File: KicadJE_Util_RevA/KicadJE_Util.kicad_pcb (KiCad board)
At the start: 2 copper layers, 268.5 x 128 mm, 225 parts, among them J101 Out1, J102 Out2, J103 In1.1, J104 In1.2, J105 In1.3, J106 SS_In2, J201 Out2.1, J202 Out2.2, J203 In2.1, J204 CV2.1, J205 In2.2, J206 CV2.2, J301 In3.1, J302 Out3.1, J303 Out3.2, P101 HEADER_2x5_Doepfer, P201 HEADER_2x5_Doepfer, P301 HEADER_2x5_Doepfer, U101 TL072, U102 TL072, U201 TL072, U202 TL072, U301 TL072, U302 TL072

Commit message: CV Module placed
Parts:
- added H201: ON, AJ:LED_Hole_3mm, F.Cu at (6.18, -1.42)
- added H202: MountingHole_Pad, AJ:MountingHole_Eurorack3, F.Cu at (-9.10, -1.15)
- added H203: MountingHole_Pad, AJ:MountingHole_Eurorack3, F.Cu at (1.95, -12.2)
- added H204: MountingHole_Pad, AJ:MountingHole_Eurorack3, F.Cu at (-1.10, -1.15)
- added H205: MountingHole_Pad, AJ:MountingHole_Eurorack3, F.Cu at (1.95, -7.20)
- added H302: MountingHole_Pad, AJ:MountingHole_Eurorack3, F.Cu at (24.9, -23.2)
- added H303: MountingHole_Pad, AJ:MountingHole_Eurorack3, F.Cu at (16.9, -18.2)
- added H304: MountingHole_Pad, AJ:MountingHole_Eurorack3, F.Cu at (24.9, -18.2)
- added H305: MountingHole_Pad, AJ:MountingHole_Eurorack3, F.Cu at (16.9, -23.2)
- added TP101: Tri, AJ:Jack_6m3, F.Cu at (70.4, -5.51)
- added TP104: In2, AJ:Jack_6m3, F.Cu at (59.3, -5.51)
- added TP106: SS, AJ:Jack_6m3, F.Cu at (48.3, -5.51)
- added TP108: OFF2, AJ:Pot_6m3_scale1, F.Cu at (50.8, -19.1)
- added TP109: Gain2, AJ:Pot_6m3_scale1, F.Cu at (82.9, -19.1)
- added TP110: Gain1, AJ:Pot_6m3_scale1, F.Cu at (66.8, -19.1)
- added TP201: Tri, AJ:Jack_6m3, F.Cu at (-7.57, -9.17)
- added TP202: SQ, AJ:Jack_6m3, F.Cu at (2.43, -20.2)
- added TP203: In1, AJ:Jack_6m3, F.Cu at (-18.6, -3.62)
- added TP204: In2, AJ:Jack_6m3, F.Cu at (-8.62, -20.2)
- added TP205: In3, AJ:Jack_6m3, F.Cu at (-29.7, -3.62)
- added TP206: SS, AJ:Jack_6m3, F.Cu at (-40.7, -3.62)
- added TP207: Glide1, AJ:Pot_6m3_scale1, F.Cu at (-22.2, -17.2)
- added TP208: Glide2, AJ:Pot_6m3_scale1, F.Cu at (-38.2, -17.2)
- J106: value SS_In2 -> In1.4
- TP107: value Gain -> OFF1
- moved R124 114.5 mm to (55.0, 82.0), turned to 90 degrees
- moved R123 105.8 mm to (75.5, 65.0)
- moved R126 102.0 mm to (55.0, 85.7), turned to 90 degrees
- moved R127 98.6 mm to (85.2, 85.7), turned to 90 degrees
- moved R112 98.2 mm to (64.5, 65.0), turned to 180 degrees
- moved C105 95.7 mm to (56.0, 95.2), turned to 90 degrees
- moved C103 94.5 mm to (76.0, 95.2), turned to 90 degrees
- moved R129 92.8 mm to (87.5, 96.3), turned to 270 degrees
- moved R131 92.1 mm to (87.5, 100.0), turned to 90 degrees
- moved R111 88.6 mm to (54.2, 104.0), turned to 90 degrees
- moved R128 85.9 mm to (67.5, 96.2), turned to 270 degrees
- moved R125 84.9 mm to (85.2, 82.0), turned to 90 degrees
- moved C106 84.0 mm to (84.0, 104.8), turned to 90 degrees
- moved R122 83.4 mm to (73.0, 104.0), turned to 90 degrees
- moved C104 81.1 mm to (64.2, 104.8), turned to 90 degrees
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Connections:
- RV101 pad 1: -12VA -> +12VA
- RV101 pad 3: +12VA -> -12VA
- RV103 pad 1: Net-(R127-Pad1) -> Inv2
- RV103 pad 3: Inv2 -> Net-(R127-Pad1)
- RV104 pad 1: -12VA -> +12VA
- RV104 pad 3: +12VA -> -12VA
- U101 pad 1: Out2 -> Net-(R128-Pad2)
- U101 pad 2: Net-(R117-Pad1) -> Inv1
- U101 pad 3: Net-(R122-Pad2) -> In1
- U102 pad 1: Net-(R128-Pad2) -> Net-(R129-Pad2)
- U102 pad 2: Inv1 -> Inv2
- U102 pad 3: In1 -> In2
- U102 pad 5: In2 -> Net-(R122-Pad2)
- U102 pad 6: Inv2 -> Net-(R117-Pad1)
- U102 pad 7: Net-(R129-Pad2) -> Out2
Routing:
- net +12VA: track 95.2 -> 76.5 mm
- net In3.1a: track 40.1 -> 25.1 mm, vias 2 -> 1
- net Out3.1: track 60.6 -> 47.5 mm
- net Net-(R316-Pad2): track 22.4 -> 10.1 mm
- net -12VA: track 80.6 -> 69.2 mm
- net Net-(R315-Pad2): track 5.28 -> 0.00 mm
- net In3.1: track 4.95 -> 0.00 mm
- net Net-(D304-Pad2): track 12.2 -> 8.72 mm
- net Net-(J303-PadT): track 10.7 -> 9.77 mm

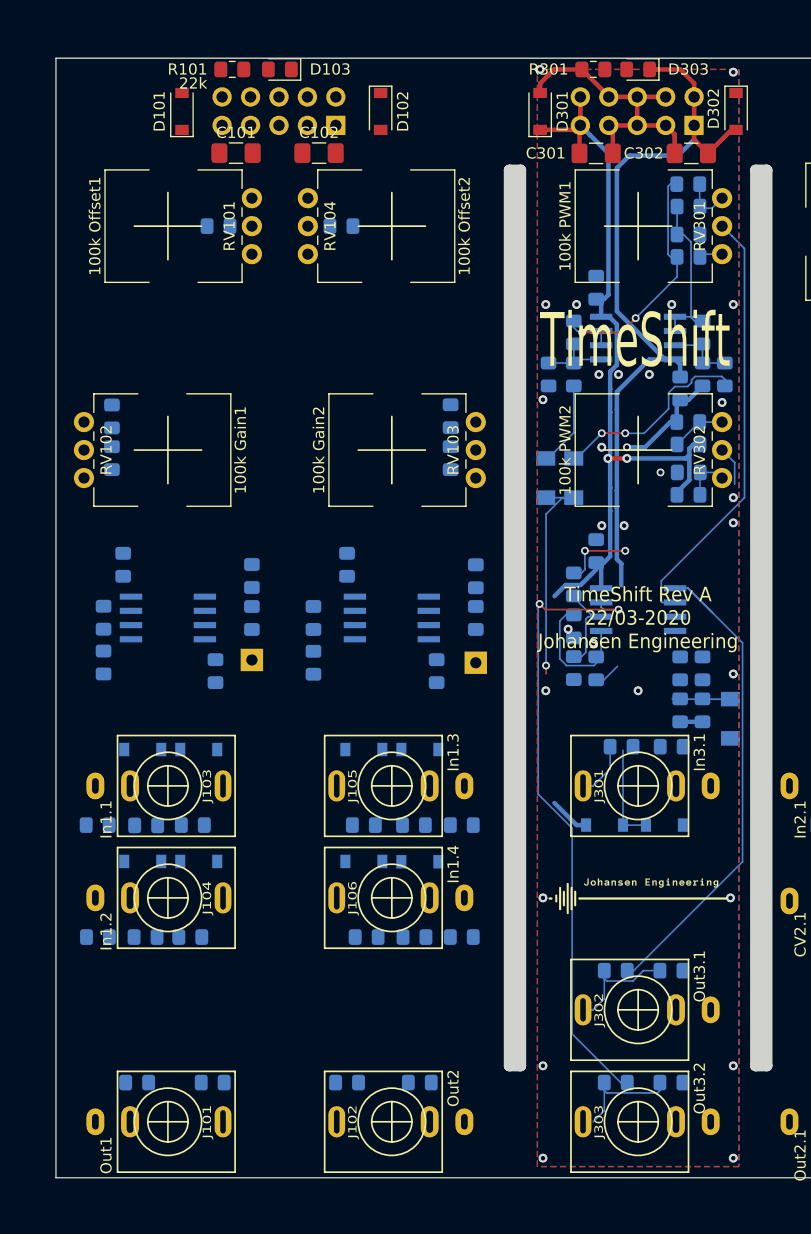
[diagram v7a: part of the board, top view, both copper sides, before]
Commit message: CV Util routed - and Timeshift fixed?
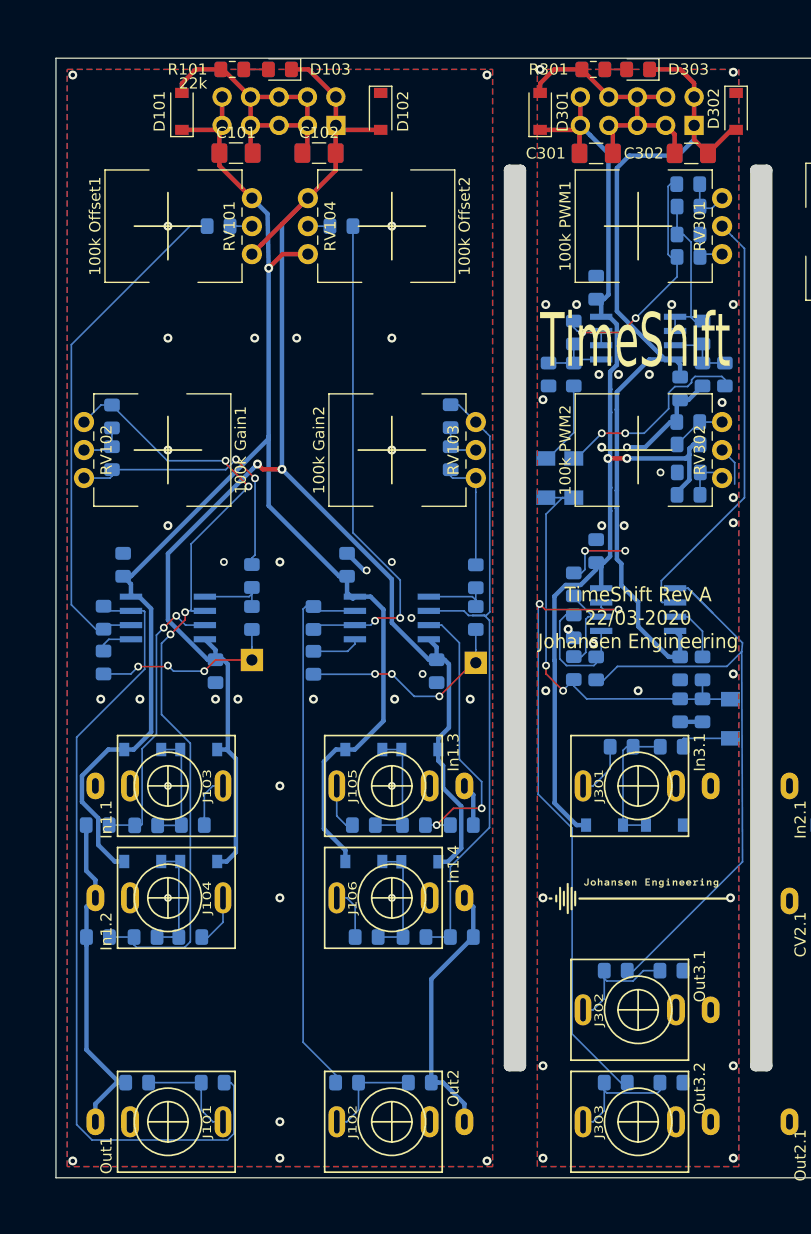
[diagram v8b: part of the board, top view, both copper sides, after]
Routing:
- net -12VA: track 69.2 -> 228.0 mm, vias 0 -> 2
- net +12VA: track 76.5 -> 233.9 mm, vias 2 -> 3
- net GND: track 39.1 -> 128.9 mm, vias 28 -> 62
- net Inv1: track 0.00 -> 74.3 mm, vias 0 -> 4
- net Out1: track 0.00 -> 72.3 mm
- net Inv2: track 0.00 -> 59.7 mm
- net Out2: track 0.00 -> 48.4 mm
- net Net-(R106-Pad1): track 0.00 -> 46.1 mm
- net Net-(R117-Pad1): track 0.00 -> 44.9 mm, vias 0 -> 2
- net In2: track 0.00 -> 25.9 mm, vias 0 -> 2
- net In1: track 0.00 -> 25.8 mm, vias 0 -> 2
- net Net-(R126-Pad1): track 0.00 -> 24.8 mm, vias 0 -> 2
- net Flow2: track 0.00 -> 19.6 mm, vias 0 -> 3
- net Flow1: track 0.00 -> 16.9 mm, vias 0 -> 3
- net In3.1a: track 25.1 -> 40.9 mm, vias 1 -> 2
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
